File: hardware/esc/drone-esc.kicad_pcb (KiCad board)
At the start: 2 copper layers, 66 x 66 mm, 197 parts, among them J1 BM08B-SRSS-TB, Q1 SP40N01GHNK, Q10 SP40N01GHNK, Q11 SP40N01GHNK, Q12 SP40N01GHNK, Q13 SP40N01GHNK, Q14 SP40N01GHNK, Q15 SP40N01GHNK, Q16 SP40N01GHNK, Q17 SP40N01GHNK, Q18 SP40N01GHNK, Q19 SP40N01GHNK, Q2 SP40N01GHNK, Q20 SP40N01GHNK, Q21 SP40N01GHNK, Q22 SP40N01GHNK, Q23 SP40N01GHNK, Q24 SP40N01GHNK, Q3 SP40N01GHNK, Q4 SP40N01GHNK, Q5 SP40N01GHNK, Q6 SP40N01GHNK, Q7 SP40N01GHNK, Q8 SP40N01GHNK, Q9 SP40N01GHNK, U10 NSG2065Q, U12 INA186A3IDCKR, U13 LMR54406DBVR, U14 FTC160808S4R7MBCA, U15 TLV76733DRVR, U2 AT32F421G8U7, U4 NSG2065Q, U5 AT32F421G8U7, U6 NSG2065Q, U7 AT32F421G8U7, U8 NSG2065Q, U9 AT32F421G8U7

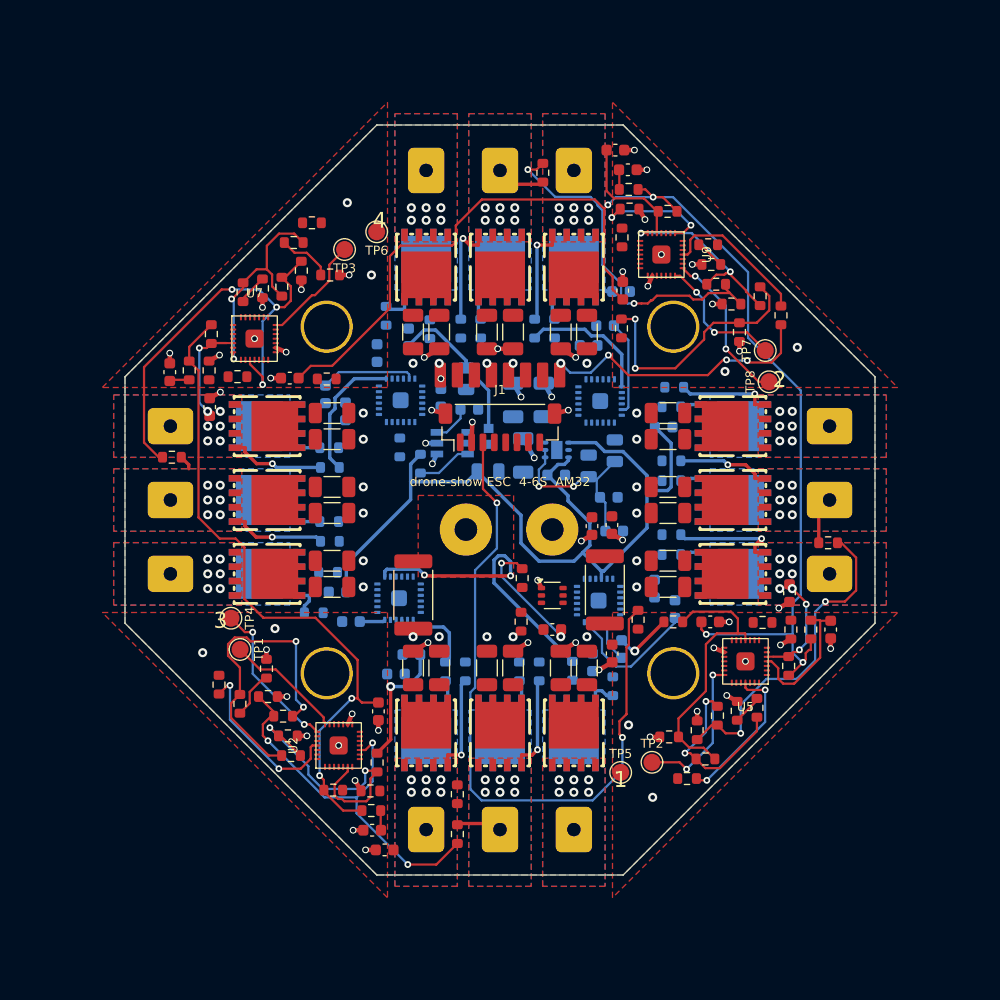
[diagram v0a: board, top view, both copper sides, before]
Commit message: ESC: grow board to 74 mm, two-pass routing, driver orientation, fanout and placement fixes
Co-Authored-By: Claude Opus 5.5 (1M context) <noreply@anthropic.com>
Claude-Session: https://claude.ai/code/session_015X7Az2AeDtDrTq19qE6e7H
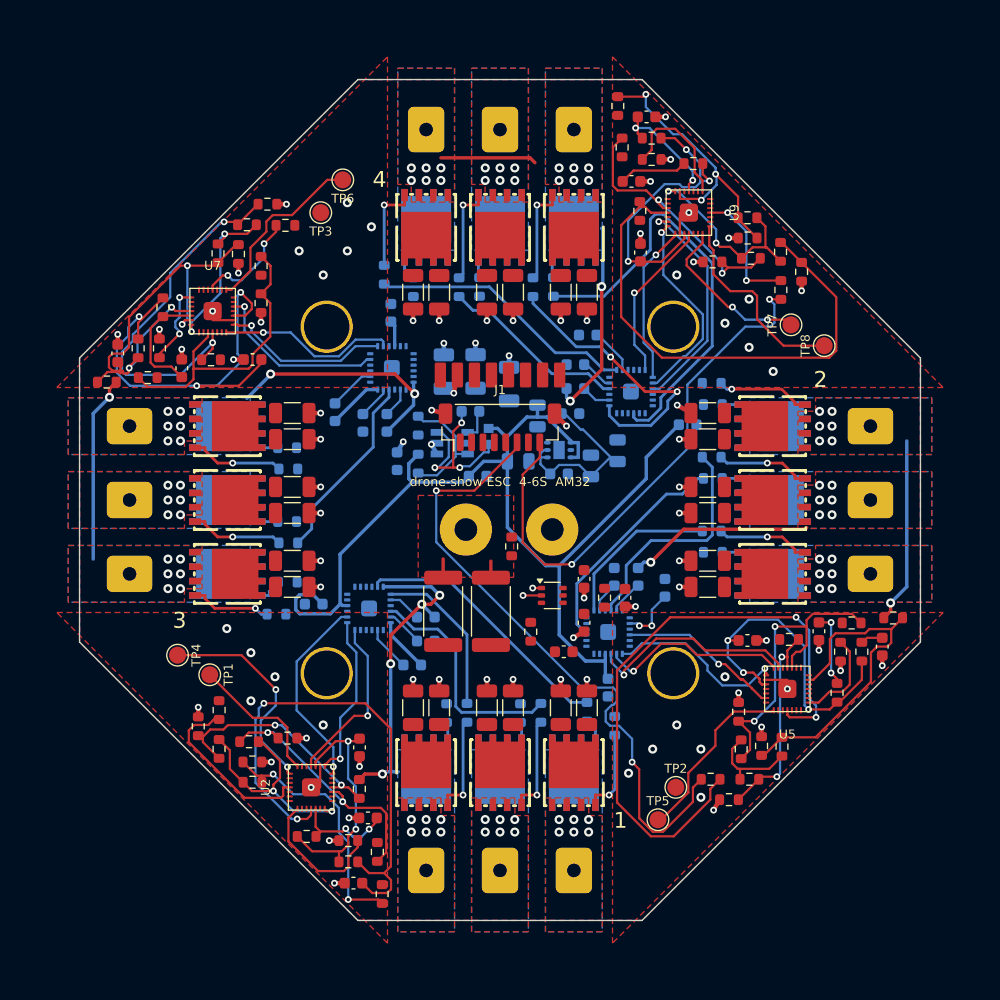
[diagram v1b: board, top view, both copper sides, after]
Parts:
- moved R27 11.6 mm to (139.6, 134.7)
- moved R66 11.6 mm to (160.4, 65.3)
- moved R48 11.5 mm to (115.4, 89.6)
- moved R12 11.5 mm to (184.6, 110.4)
- moved R72 10.5 mm to (162.3, 74.6)
- moved R54 10.3 mm to (124.6, 87.7)
- moved R36 10.3 mm to (175.4, 112.3)
- moved Rsense2 10.2 mm to (149.2, 109.8)
- moved C39 9.43 mm to (156.6, 90.2)
- moved R33 8.64 mm to (137.6, 125.4)
- moved R53 8.32 mm to (129.5, 74.0)
- moved C81 8.10 mm to (156.2, 92.4)
- moved R32 7.86 mm to (123.4, 119.9)
- moved R35 7.63 mm to (170.2, 126.4)
- moved R71 7.63 mm to (176.5, 79.9)
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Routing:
- net /CURR: track 61.8 -> 0.00 mm, vias 2 -> 0
- net +3V3: track 191.4 -> 132.6 mm, vias 8 -> 11
- net /M2: track 0.00 -> 57.0 mm, vias 0 -> 2
- net Net-(U2-NRST): track 1.74 -> 46.7 mm, vias 0 -> 2
- net Net-(U5-PB4): track 13.3 -> 54.8 mm
- net /ESC4/GLC: track 0.00 -> 38.2 mm
- net /ESC3/FBC: track 4.81 -> 32.9 mm, vias 0 -> 2
- net /ESC2/FBA: track 2.64 -> 30.0 mm
- net /ESC1/GHA: track 26.7 -> 0.00 mm, vias 2 -> 0
- net /ESC1/MotorC: track 2.26 -> 28.4 mm, vias 6 -> 10
- net /ESC3/FBA: track 2.69 -> 28.4 mm, vias 0 -> 2
- net /ESC4/GHA: track 0.00 -> 23.6 mm
- net /ESC4/FBC: track 22.2 -> 45.8 mm, vias 2 -> 0
- net /ESC1/GLA: track 0.00 -> 23.4 mm
- net /M4: track 24.6 -> 47.7 mm, vias 4 -> 2
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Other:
- board size 66 x 66 mm -> 74 x 74 mm

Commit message: esc: 4-layer stackup (GND plane, +BATT pour), PCBWay 2 oz rules, one-pass routing
Inner GND plane on In1 and a +BATT pour on In2 that signals may cross.
Phase strips go into the DSN as protected copper so one Freerouting pass
routes everything; low-side source tabs and fanout vias on every GND/+BATT
pad replace the outer-pour islands. Track/space 0.178/0.2 mm, vias
0.66/0.3 mm for 7 mil annular ring at 2 oz. Board is still a work in
progress: routing is not complete yet.

Co-Authored-By: Claude Opus 5.5 (1M context) <noreply@anthropic.com>
Claude-Session: https://claude.ai/code/session_015X7Az2AeDtDrTq19qE6e7H
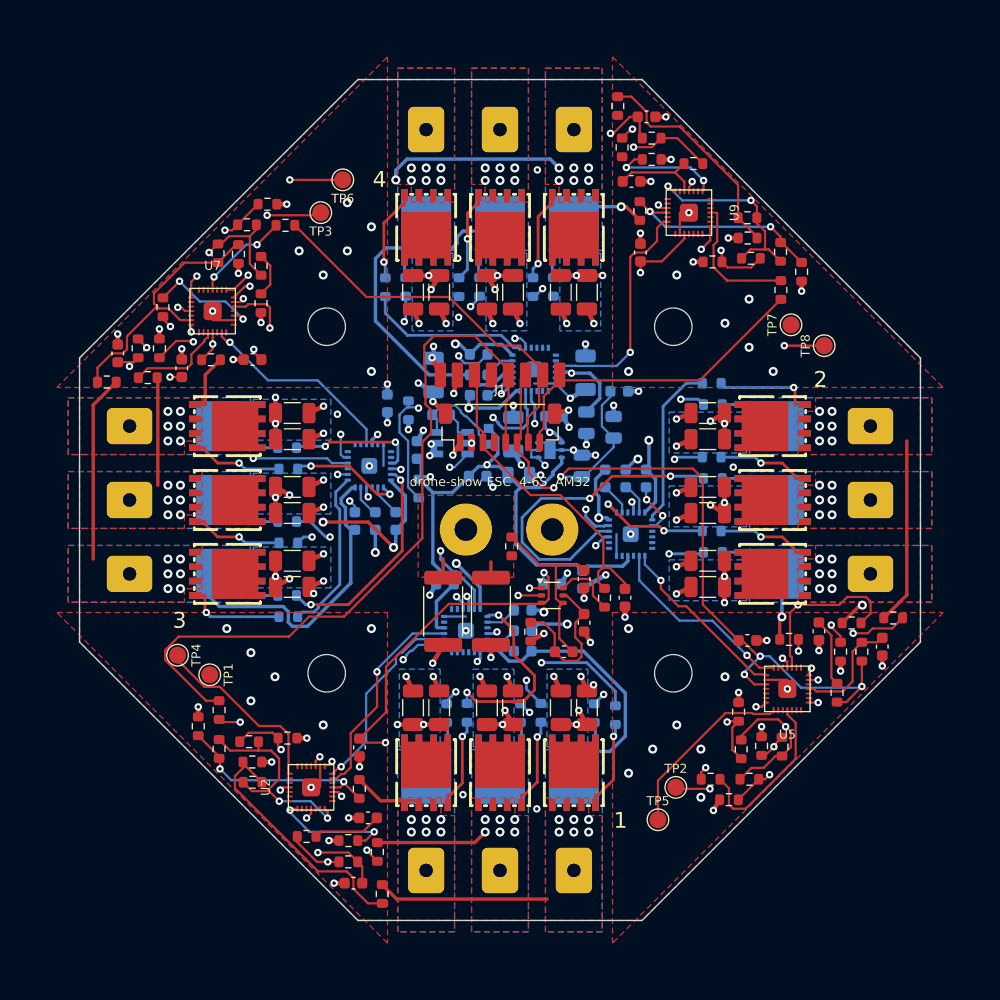
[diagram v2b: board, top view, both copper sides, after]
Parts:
- moved C63 12.3 mm to (142.7, 95.6)
- moved C68 11.8 mm to (154.7, 92.6)
- moved C57 11.7 mm to (145.2, 107.4)
- moved C53 9.80 mm to (152.0, 113.3)
- moved C58 9.77 mm to (157.3, 107.0)
- moved C56 9.77 mm to (162.9, 98.1)
- moved C67 9.75 mm to (148.1, 87.2)
- moved C62 9.73 mm to (137.2, 101.8)
- moved C93 9.72 mm to (154.6, 107.4)
- moved U6 8.84 mm to (161.5, 103.0)
- moved U8 8.84 mm to (138.5, 97.0)
- moved U10 8.74 mm to (153.0, 88.5)
- moved U4 8.74 mm to (147.0, 111.5)
- moved C33 8.73 mm to (161.1, 98.1)
- moved C34 8.71 mm to (139.0, 101.8)
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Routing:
- net +3V3: track 132.6 -> 243.2 mm, vias 11 -> 15
- net /M1: track 0.00 -> 66.8 mm
- net /ESC4/MotorC: track 17.7 -> 62.0 mm, vias 8 -> 9
- net /ESC3/MotorB: track 0.00 -> 44.2 mm, vias 6 -> 7
- net GND: track 66.8 -> 108.9 mm, vias 85 -> 119
- net +BATT: track 5.14 -> 47.2 mm, vias 5 -> 35
- net Net-(U5-PB4): track 54.8 -> 15.0 mm, vias 2 -> 0
- net /ESC4/GLC: track 38.2 -> 0.00 mm
- net Net-(U2-NRST): track 46.7 -> 10.3 mm
- net /M3: track 0.00 -> 34.1 mm
- net /ESC1/MotorB: track 0.00 -> 32.4 mm, vias 6 -> 7
- net /ESC2/MotorC: track 0.00 -> 31.7 mm, vias 6 -> 8
- net /ESC1/MotorA: track 4.83 -> 36.2 mm
- net /ESC4/MotorB: track 0.00 -> 30.3 mm
- net /CURR: track 0.00 -> 28.4 mm
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- added copper zone on In2.Cu, net +BATT
- added copper zone on In1.Cu, net GND
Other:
- copper layers 2 -> 4

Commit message: esc: 80 mm board, clean-up router, fab exports; 19 connections still open
Board grows to 80 mm, FC wire pads dropped (J1 carries the signals),
gate/phase/supply tracks narrowed to 0.2/0.25 mm. Freerouting leaves
~20 connections open round the MCUs and gate drivers; tools/rescue_*.py
adds a grid maze router that finishes some of them. 19 remain and are
listed in the README; fab/ is from this unfinished board.

Co-Authored-By: Claude Opus 5.5 (1M context) <noreply@anthropic.com>
Claude-Session: https://claude.ai/code/session_015X7Az2AeDtDrTq19qE6e7H
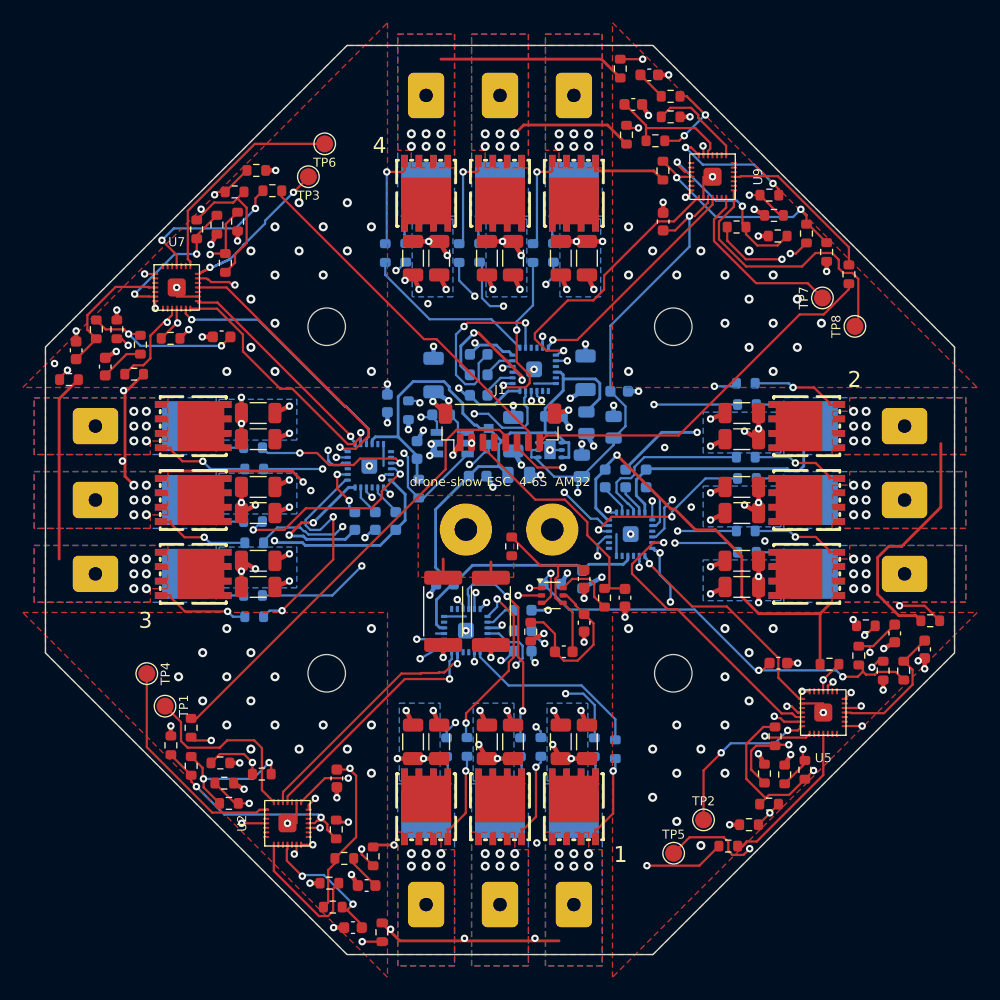
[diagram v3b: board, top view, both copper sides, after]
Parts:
- moved R50 7.47 mm to (126.9, 75.5)
- moved C65 6.78 mm to (161.7, 65.2)
- moved C60 6.73 mm to (115.3, 88.3)
- moved C54 6.67 mm to (184.7, 111.7)
- moved R29 6.30 mm to (125.4, 123.1)
- moved R68 6.17 mm to (174.4, 76.8)
- moved R87 6.14 mm to (180.7, 80.1)
- moved R39 6.08 mm to (170.1, 130.5)
- moved C48 5.95 mm to (138.3, 133.9)
- moved R14 5.89 mm to (173.3, 124.1)
- moved TP1 4.80 mm to (120.5, 118.1)
- moved R18 4.21 mm to (135.3, 135.8)
- moved R36 4.17 mm to (179.0, 114.5)
- moved R33 4.10 mm to (135.6, 129.0)
- moved R41 4.10 mm to (116.3, 85.0)
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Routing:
- net +3V3: track 243.2 -> 198.6 mm, vias 15 -> 10
- net /ESC2/AH: track 0.00 -> 32.8 mm, vias 0 -> 2
- net /M1: track 66.8 -> 40.4 mm
- net /ESC2/BH: track 0.00 -> 25.6 mm, vias 0 -> 1
- net /ESC3/CH: track 0.00 -> 24.6 mm, vias 0 -> 1
- net /ESC4/AL: track 0.00 -> 24.3 mm, vias 0 -> 1
- net /ESC3/BL: track 0.00 -> 22.9 mm, vias 0 -> 1
- net /ESC4/MotorC: track 62.0 -> 39.6 mm, vias 9 -> 7
- net /ESC1/BH: track 0.00 -> 21.9 mm, vias 0 -> 1
- net /ESC2/CH: track 0.00 -> 21.7 mm, vias 0 -> 3
- net /ESC1/CH: track 0.00 -> 21.5 mm, vias 0 -> 1
- net /ESC4/CH: track 0.00 -> 20.8 mm, vias 0 -> 1
- net /ESC4/CL: track 20.7 -> 0.00 mm, vias 1 -> 0
- net /ESC4/BL: track 0.00 -> 20.5 mm, vias 0 -> 2
- net /ESC3/AL: track 0.00 -> 19.7 mm, vias 0 -> 1
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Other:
- board size 74 x 74 mm -> 80 x 80 mm

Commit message: esc: battery and FC connector on the corner flats, MCUs beside their drivers; DRC clean
Layout
* Battery pads on the rear-right corner flat: 7 x 6 mm plated pads, bare on
  both sides, 2.2 mm hole and a ring of eight small plated holes each, so the
  lead goes on one side and the bulk electrolytic on the other. The shunts
  sit beside BAT+, the INA186 under them; its output filter is under J1.
* J1 (side-entry JST SH) on the front-left corner flat, opening outward.
* Each MCU on the bottom on the centre side of its gate driver, 6 mm from the
  board centre, so the six PWM lines are a few mm long on one layer. NRST,
  BOOT0, VDDA, 3V3 decoupling and SWD test points on top over the MCU.
* 10 V / 3.3 V supplies on the bottom of the rear-left corner.
* Board stays 80 mm across the flats.

Routing
* The MCU, driver and the caps round them are placed exactly and their
  escapes (PWM lines, 3V3/NRST/VDDA/back-EMF escapes, the driver's high-side
  row with gate vias) are drawn by route_prep.pwm_lines in every channel:
  neither router gets out of the 0.4/0.5 mm pitch pins reliably.
* New pre-route step: rescue_route.py routes the MCU's local nets, the
  bootstrap nets and 3V3 on the near-empty board (tools/local_nets.py picks
  them), and Freerouting gets them as protected wiring. DSN clearance 205 um
  so Freerouting's rounding stays above the 0.2 mm minimum.
* build.sh runs on macOS with KiCad 10's bundled Python (KIPY) and a plain
  Python for the netlist and maze router (PYTHON); `build.sh place` stops
  after placement.

DRC: 0 errors, 0 unconnected. Warnings: U3 schematic parity (expected), the
schematic's empty LCSC fields, a few dangling stubs and pour slivers.
README and fab/ updated, including frame notes for the corner exits.

Co-Authored-By: Claude Opus 5.5 (1M context) <noreply@anthropic.com>
Claude-Session: https://claude.ai/code/session_015X7Az2AeDtDrTq19qE6e7H
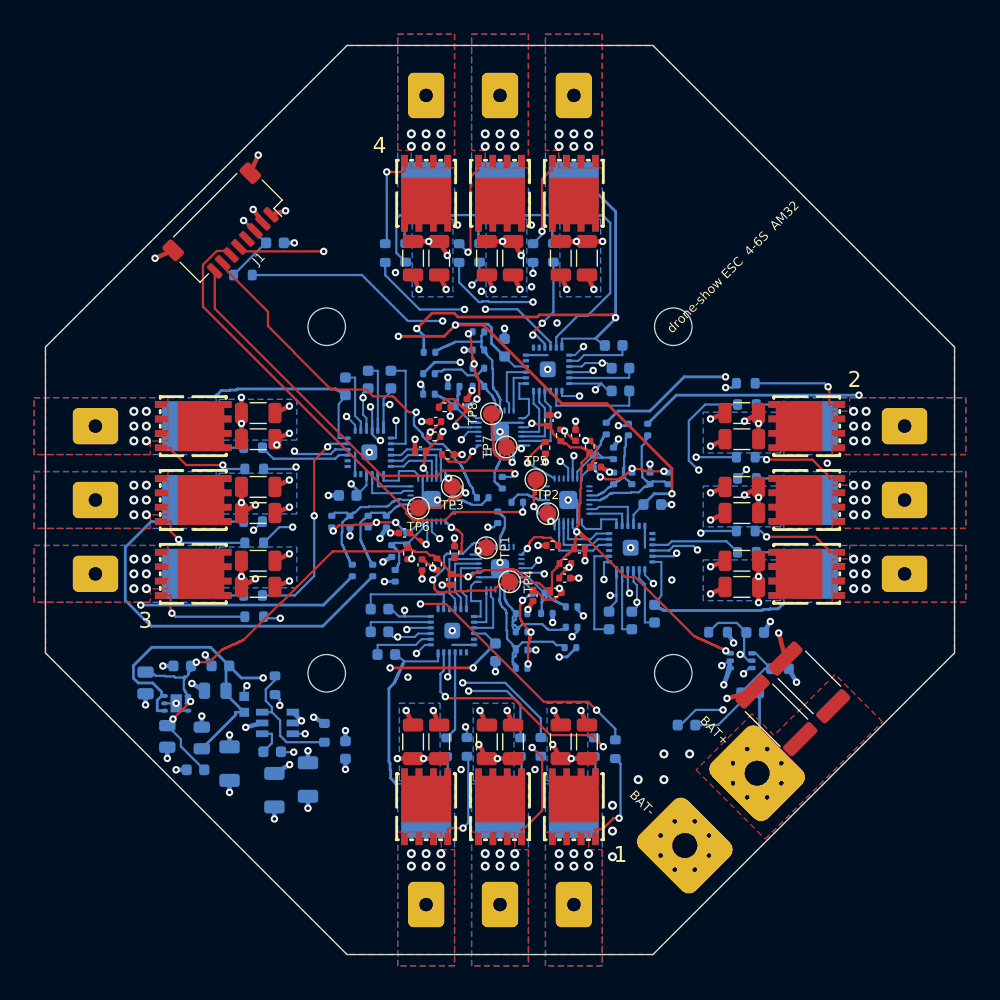
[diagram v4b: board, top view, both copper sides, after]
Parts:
- C40, C41, C42, C94, R73, R89, R90, U12, U2, U5, U7, U9: moved to B.Cu
- C48, C49, C50, C52, C54, C55, C59, C60, C61, C64, C65, C66: footprint Capacitor_SMD:C_0603_1608Metric -> Capacitor_SMD:C_0402_1005Metric
- J1: value BM08B-SRSS-TB -> SM08B-SRSS-TB; footprint drone-esc:JST_SH_BM08B-SRSS-TB_Vertical -> drone-esc:JST_SH_SM08B-SRSS-TB_Horizontal
- R10, R11, R12, R13, R14, R15, R20, R25, R26, R27, R28, R29, R30, R31, R32, R33, R34, R35, R36, R39, R46, R47, R48, R49, R50, R51, R52, R53, R54, R57, R64, R65, R66, R67, R68, R69, R70, R71, R72, R87: footprint Resistor_SMD:R_0603_1608Metric -> Resistor_SMD:R_0402_1005Metric; moved to B.Cu
- R18, R19, R21, R22, R40, R41, R58, R59, R84, R85, R86, R88: footprint Resistor_SMD:R_0603_1608Metric -> Resistor_SMD:R_0402_1005Metric
- moved C81 50.0 mm to (123.2, 123.7), turned to 180 degrees
- moved C51 47.8 mm to (120.7, 120.8), turned to 90 degrees
- moved C6 46.5 mm to (126.2, 123.2), turned to 90 degrees
- moved C94 43.9 mm to (130.2, 77.4), turned to 0 degrees
- moved C86 43.8 mm to (123.8, 120.9), turned to 90 degrees
- moved C4 42.9 mm to (118.8, 116.1), turned to 90 degrees
- moved R73 42.7 mm to (127.4, 80.2), turned to 0 degrees
- moved U15 39.7 mm to (121.5, 117.9), turned to 180 degrees
- moved C3 37.7 mm to (130.1, 125.5), turned to 90 degrees
- moved C2 37.3 mm to (133.1, 124.6), turned to 90 degrees
- moved R21 36.6 mm to (155.4, 94.3)
- moved R18 36.5 mm to (155.7, 105.6)
- moved R58 36.4 mm to (144.3, 94.4)
- moved R40 36.4 mm to (144.5, 105.7)
- moved C52 36.0 mm to (156.7, 94.3), turned to 90 degrees
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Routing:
- net +3V3: track 198.6 -> 113.2 mm
- net +10V: track 84.8 -> 151.7 mm, vias 0 -> 8
- net Net-(U12-OUT): track 5.67 -> 69.8 mm, vias 0 -> 2
- net /ESC3/MotorA: track 43.9 -> 69.2 mm
- net /ESC2/AH: track 32.8 -> 8.48 mm, vias 2 -> 0
- net /ESC3/MotorB: track 39.7 -> 60.1 mm, vias 10 -> 7
- net /ESC4/AL: track 24.3 -> 5.12 mm, vias 1 -> 0
- net /ESC3/CH: track 24.6 -> 5.39 mm, vias 1 -> 0
- net /ESC2/BH: track 25.6 -> 6.88 mm, vias 1 -> 0
- net Net-(U5-PA14): track 23.2 -> 4.68 mm, vias 2 -> 1
- net /ESC3/BL: track 22.9 -> 4.50 mm, vias 1 -> 0
- net /ESC4/FBCOMMON: track 27.9 -> 10.0 mm, vias 4 -> 3
- net Net-(U9-PA14): track 24.3 -> 6.99 mm, vias 0 -> 1
- net /ESC1/BL: track 21.3 -> 4.38 mm, vias 2 -> 0
- net /ESC2/FBA: track 24.1 -> 7.38 mm, vias 2 -> 0
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- removed copper zone on F.Cu, net GND
